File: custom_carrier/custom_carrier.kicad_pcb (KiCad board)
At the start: 4 copper layers, 70 x 75 mm, 20 parts, among them J1 ERF5-040-05.0-X-DV, J13 PJ-002AH-SMT-TR, J14 87832-1420, J2 ERF5-040-05.0-X-DV, J3 ERF5-040-05.0-X-DV, J4 ERF5-040-05.0-X-DV, J5 45230-220230, J6 45230-220230

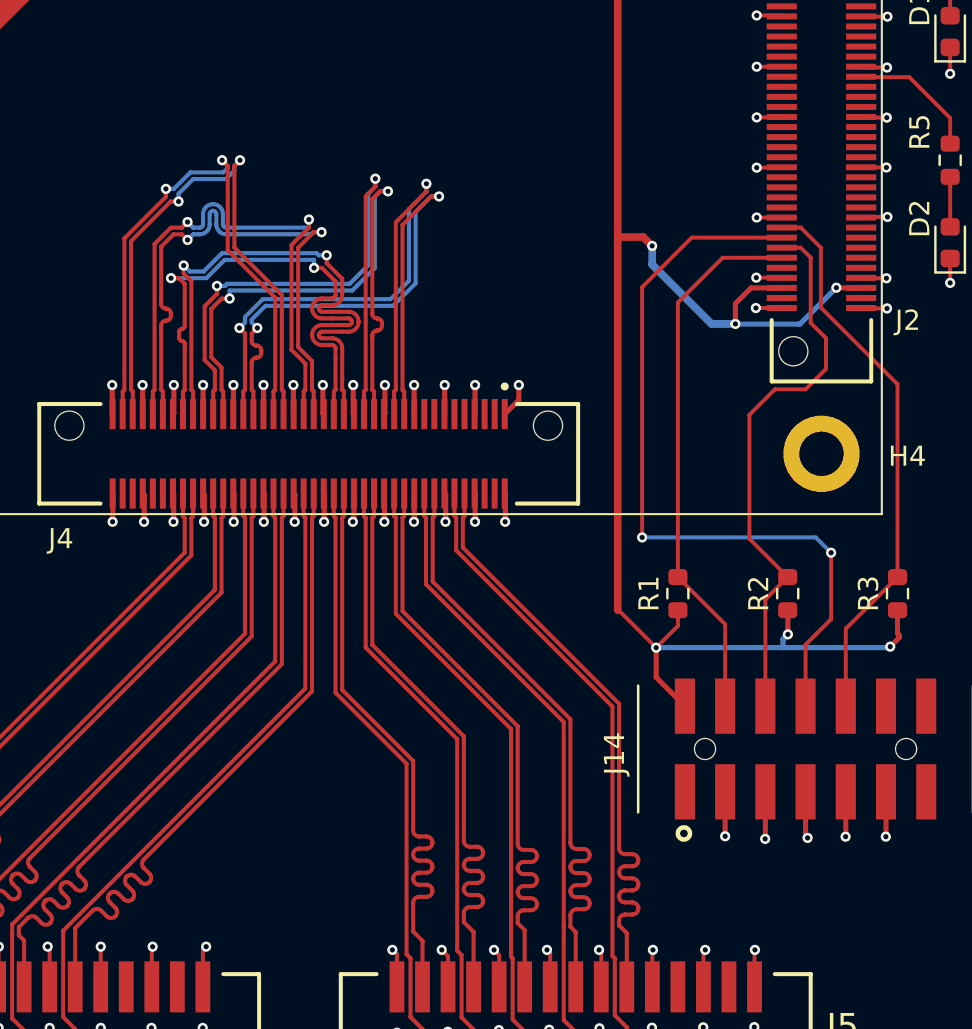
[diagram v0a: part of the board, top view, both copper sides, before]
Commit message: fixed loopback wiring error, increased Revision from A-1 to B-1
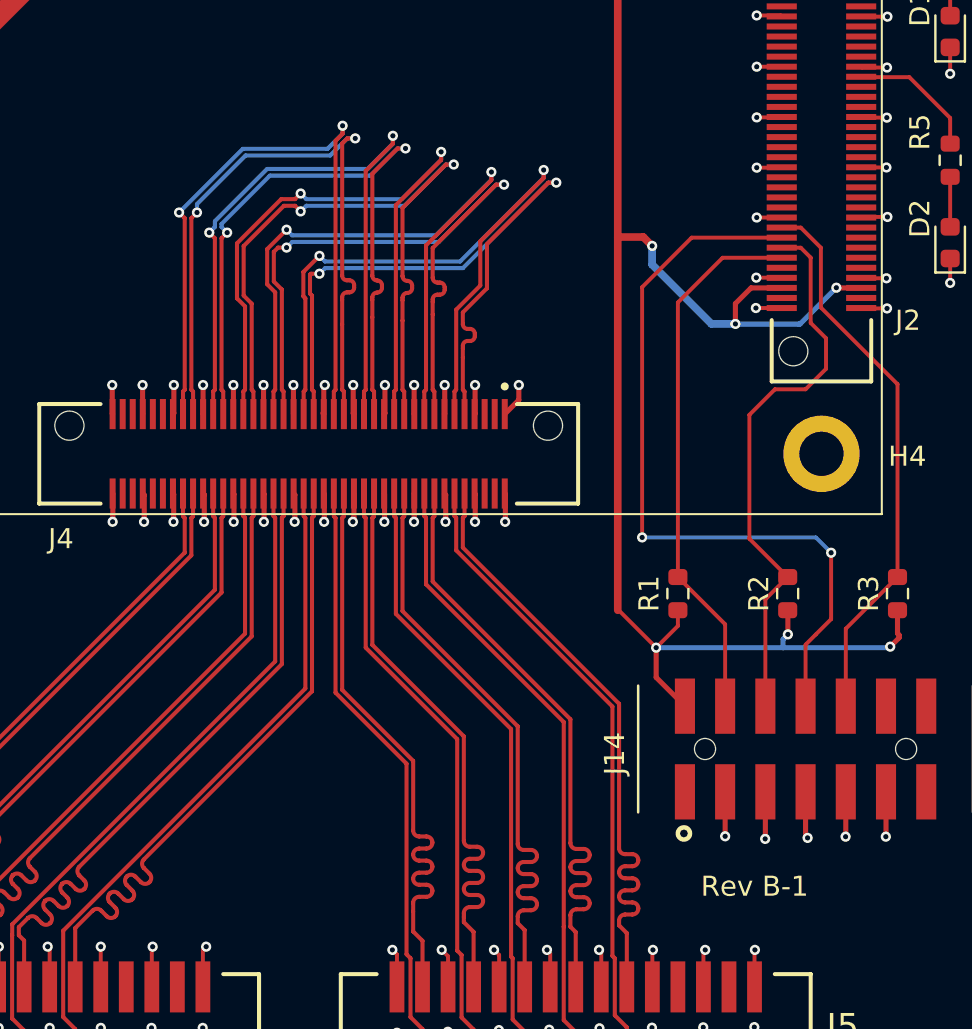
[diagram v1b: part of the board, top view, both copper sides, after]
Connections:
- J4 pad 09: unconnected-(J4-Pad09) -> /CH0_DCO_P
- J4 pad 11: unconnected-(J4-Pad11) -> /CH0_DCO_N
- J4 pad 15: unconnected-(J4-Pad15) -> /CH0_D3_P
- J4 pad 17: unconnected-(J4-Pad17) -> /CH0_D3_N
- J4 pad 21: /CH0_DCO_P -> /CH0_D2_P
- J4 pad 23: /CH0_DCO_N -> /CH0_D2_N
- J4 pad 27: /CH0_D3_P -> /CH0_D1_P
- J4 pad 29: /CH0_D3_N -> /CH0_D1_N
- J4 pad 33: /CH0_D2_P -> /CH0_D0_P
- J4 pad 35: /CH0_D2_N -> /CH0_D0_N
- J4 pad 39: /CH0_D1_P -> /CH0_DCO_P
- J4 pad 41: /CH0_D1_N -> /CH0_DCO_N
- J4 pad 45: /CH0_D0_P -> /CH0_D3_P
- J4 pad 47: /CH0_D0_N -> /CH0_D3_N
- J4 pad 51: /CH0_DCO_P -> /CH0_D2_P
- J4 pad 53: /CH0_DCO_N -> /CH0_D2_N
- J4 pad 57: /CH0_D3_P -> /CH0_D1_P
- J4 pad 59: /CH0_D3_N -> /CH0_D1_N
- J4 pad 63: /CH0_D2_P -> /CH0_D0_P
- J4 pad 65: /CH0_D2_N -> /CH0_D0_N
- J4 pad 69: /CH0_D1_P -> unconnected-(J4-Pad69)
- J4 pad 71: /CH0_D1_N -> unconnected-(J4-Pad71)
- J4 pad 75: /CH0_D0_P -> unconnected-(J4-Pad75)
- J4 pad 77: /CH0_D0_N -> unconnected-(J4-Pad77)
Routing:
- net /CH0_D2_N: track 28.5 -> 35.2 mm
- net /CH0_D2_P: track 28.5 -> 35.2 mm
- net /CH0_D1_N: track 29.2 -> 35.1 mm
- net /CH0_D1_P: track 29.2 -> 35.1 mm
- net /CH0_D0_N: track 29.8 -> 34.8 mm
- net /CH0_D0_P: track 29.8 -> 34.8 mm
- net /CH0_DCO_N: track 31.3 -> 35.6 mm
- net /CH0_DCO_P: track 31.3 -> 35.6 mm
- net /CH0_D3_P: track 31.2 -> 35.0 mm
- net /CH0_D3_N: track 31.2 -> 35.0 mm
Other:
- board text added: "Rev B-1"

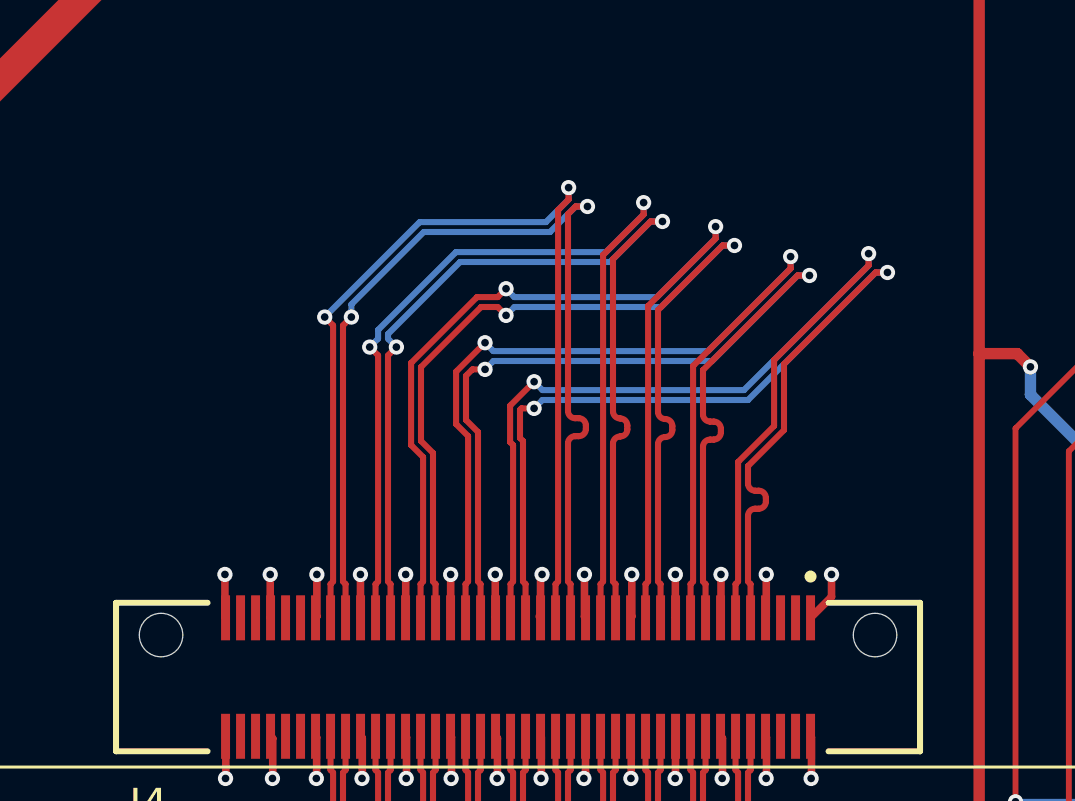
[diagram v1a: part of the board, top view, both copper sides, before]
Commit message: Rev B-1 with proper loopback pinout routed
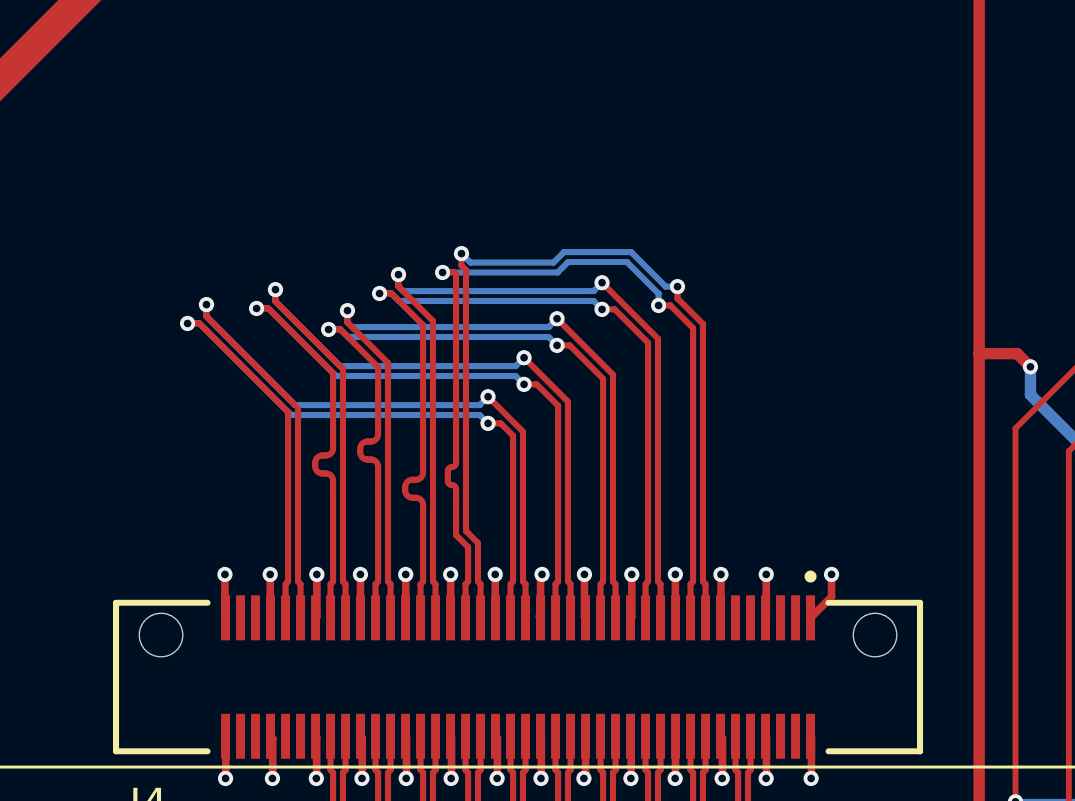
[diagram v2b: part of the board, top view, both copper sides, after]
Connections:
- J4 pad 09: /CH0_DCO_P -> unconnected-(J4-Pad09)
- J4 pad 11: /CH0_DCO_N -> unconnected-(J4-Pad11)
- J4 pad 69: unconnected-(J4-Pad69) -> /CH0_DCO_P
- J4 pad 71: unconnected-(J4-Pad71) -> /CH0_DCO_N
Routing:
- net /CH0_D1_N: track 35.1 -> 29.1 mm
- net /CH0_D1_P: track 35.1 -> 29.2 mm
- net /CH0_DCO_N: track 35.6 -> 30.0 mm
- net /CH0_DCO_P: track 35.6 -> 30.6 mm
- net /CH0_D0_N: track 34.8 -> 30.9 mm
- net /CH0_D2_N: track 35.2 -> 31.3 mm
- net /CH0_D0_P: track 34.8 -> 30.9 mm
- net /CH0_D2_P: track 35.2 -> 31.3 mm
- net /CH0_D3_N: track 35.0 -> 31.8 mm
- net /CH0_D3_P: track 35.0 -> 31.8 mm

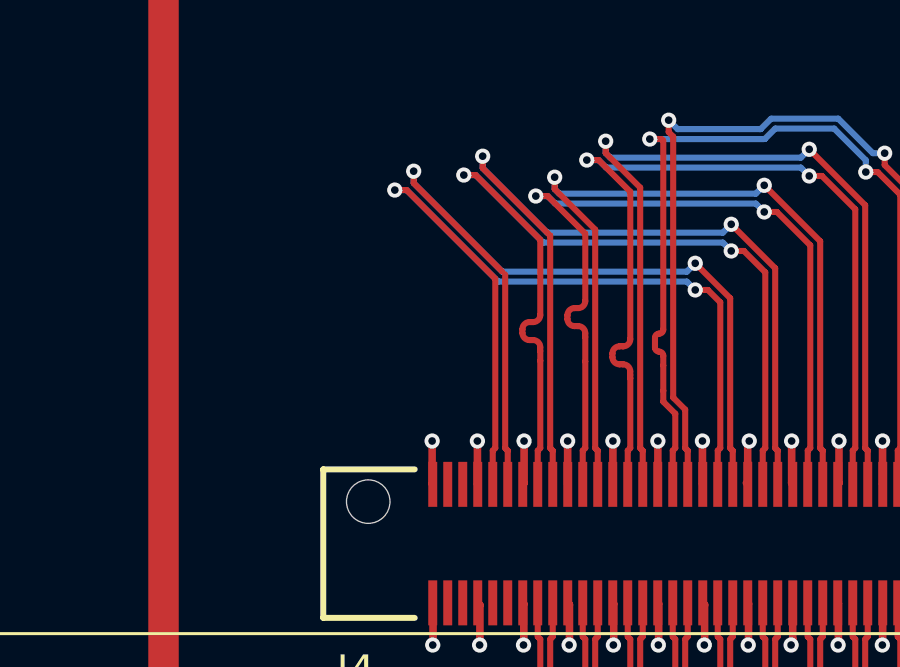
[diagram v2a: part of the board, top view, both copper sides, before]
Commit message: tuned loopback diff lengths
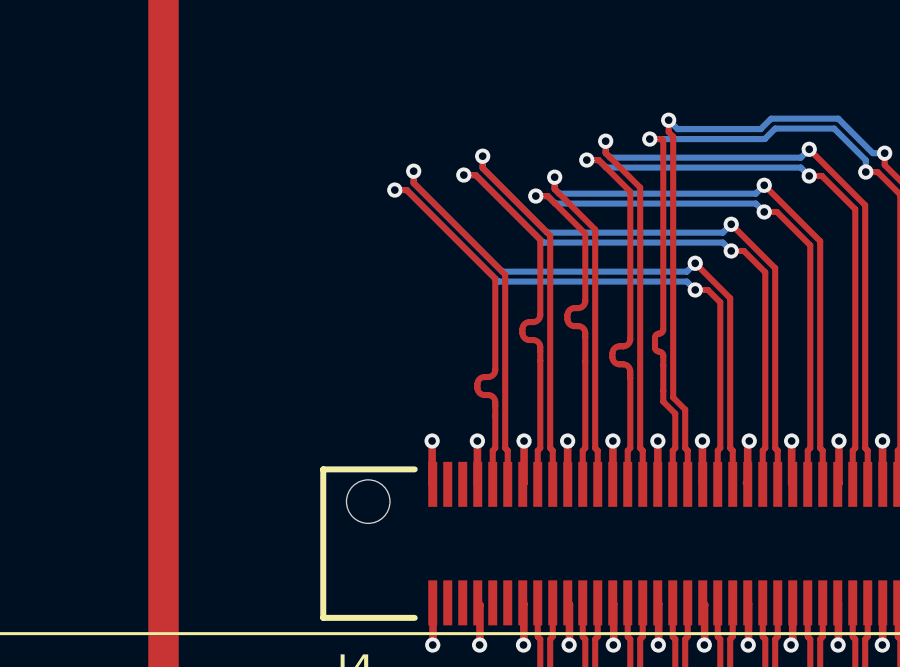
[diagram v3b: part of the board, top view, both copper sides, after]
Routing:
- net /CH0_DCO_N: track 30.0 -> 30.7 mm
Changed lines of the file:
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@@
 	)
 	(segment
-		(start 124.1651 113.815099)
-		(end 124.1651 108.031612)
-		(width 0.2032)
-		(layer "F.Cu")
-		(net 25)
-	)
-	(segment
 		(start 131.75 113.899999)
 		(end 131.75 115.025)
@@
 	)
 	(segment
-		(start 124.068387 107.9349)
-		(end 121.114309 104.980822)
+		(start 124.1651 113.815099)
+		(end 124.1651 108.031613)
 		(width 0.2032)
 		(layer "F.Cu")
@@
 	)
 	(segment
+		(start 124.1651 108.031613)
+		(end 121.114309 104.980822)
+		(width 0.2032)
+		(layer "F.Cu")
+		(net 25)
+	)
+	(segment
 		(start 124.25 115.025)
 		(end 124.25 113.899999)
@@
 	)
 	(segment
+		(start 120.880822 105.214309)
+		(end 123.8349 108.168387)
+		(width 0.2032)
+		(layer "F.Cu")
+		(net 37)
+	)
+	(segment
 		(start 131.25 113.899999)
 		(end 131.25 115.025)
@@
 	)
 	(segment
+		(start 123.479562 112.046726)
+		(end 123.5949 112.046726)
+		(width 0.2032)
+		(layer "F.Cu")
+		(net 37)
+	)
+	(segment
+		(start 123.8349 112.739431)
+		(end 123.8349 113.815099)
+		(width 0.2032)
+		(layer "F.Cu")
+		(net 37)
+	)
+	(segment
 		(start 131.3349 108.957374)
 		(end 131.3349 113.815099)
@@
 	)
 	(segment
-		(start 123.8349 108.168387)
+		(start 120.485691 105.214309)
 		(end 120.880822 105.214309)
 		(width 0.2032)
@@
 	)
 	(segment
+		(start 123.8349 112.406726)
+		(end 123.8349 112.739431)
+		(width 0.2032)
+		(layer "F.Cu")
+		(net 37)
+	)
+	(segment
+		(start 123.5949 111.446726)
+		(end 123.479562 111.446726)
+		(width 0.2032)
+		(layer "F.Cu")
+		(net 37)
+	)
+	(segment
 		(start 123.75 113.899999)
-		(end 123.8349 113.815099)
+		(end 123.75 115.025)
 		(width 0.2032)
 		(layer "F.Cu")
@@
 	)
 	(segment
-		(start 120.880822 105.214309)
-		(end 120.485691 105.214309)
+		(start 123.239562 111.686726)
+		(end 123.239562 111.806726)
 		(width 0.2032)
 		(layer "F.Cu")
@@
 	)
 	(segment
-		(start 123.75 115.025)
-		(end 123.75 113.899999)
+		(start 123.8349 112.286726)
+		(end 123.8349 112.406726)
 		(width 0.2032)
 		(layer "F.Cu")
@@
 	(segment
 		(start 123.8349 113.815099)
-		(end 123.8349 108.168387)
+		(end 123.75 113.899999)
+		(width 0.2032)
+		(layer "F.Cu")
+		(net 37)
+	)
+	(segment
+		(start 123.8349 108.168387)
+		(end 123.8349 111.206726)
 		(width 0.2032)
 		(layer "F.Cu")
@@
 		(net 37)
 	)
+	(arc
+		(start 123.5949 112.046726)
+		(mid 123.764606 112.11702)
+		(end 123.8349 112.286726)
+		(width 0.2032)
+		(layer "F.Cu")
+		(net 37)
+	)
+	(arc
+		(start 123.8349 111.206726)
+		(mid 123.764606 111.376432)
+		(end 123.5949 111.446726)
+		(width 0.2032)
+		(layer "F.Cu")
+		(net 37)
+	)
+	(arc
+		(start 123.479562 111.446726)
+		(mid 123.309856 111.51702)
+		(end 123.239562 111.686726)
+		(width 0.2032)
+		(layer "F.Cu")
+		(net 37)
+	)
+	(arc
+		(start 123.239562 111.806726)
+		(mid 123.309856 111.976432)
+		(end 123.479562 112.046726)
+		(width 0.2032)
+		(layer "F.Cu")
+		(net 37)
+	)
 	(segment
 		(start 123.931613 108.2651)
@@
 	)
 	(generated
+		(type tuning_pattern)
+		(name "Tuning Pattern")
+		(layer "F.Cu")
+		(base_line
+			(pts
+				(xy 123.8349 111.206726) (xy 123.8349 112.739431)
+			)
+		)
+		(base_line_coupled
+			(pts
+				(xy 124.1651 111.206726) (xy 124.1651 111.197493)
+			)
+		)
+		(corner_radius_percent 80)
+		(end
+			(xy 123.8349 112.739431)
+		)
+		(initial_side "right")
+		(last_diff_pair_gap 0.18)
+		(last_netname "/CH0_DCO_N")
+		(last_status "tuned")
+		(last_track_width 0.2032)
+		(last_tuning "-0.0000 mm (tuned)")
+		(max_amplitude 1)
+		(min_amplitude 0.2)
+		(min_spacing 0.6)
+		(origin
+			(xy 123.8349 111.206726)
+		)
+		(override_custom_rules no)
+		(rounded yes)
+		(single_sided no)
+		(target_length 1000000)
+		(target_length_max 1000000.1)
+		(target_length_min 999999.9)
+		(target_skew 0)
+		(target_skew_max 0.1)
+		(target_skew_min -0.1)
+		(tuning_mode "diff_pair_skew")
+		(members 127e52eb-aa4b-4102-889c-6d42faf09a84 4aee5919-594c-4d2f-9088-ff908704a2b3
+			73cbbcd1-c357-421e-ad6a-378d5ffddb81 76f127d9-31d6-4f8f-b22d-c2fb56041dd8
+			a2052162-17dc-4daf-97cc-ac9123469ba4 bdf9e75e-00b3-41a1-a4bb-76a61626ef4c
+			d76653c5-0642-4209-a656-6c63872a9f66 dfed89ed-d11c-4731-86b7-0eb0fb3e2621
+			e54c6c92-3189-44ae-b87a-12d588a70754
+		)
+	)
+	(generated
